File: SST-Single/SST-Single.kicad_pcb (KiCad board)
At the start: 2 copper layers, 62 x 24 mm, 13 parts, among them J1 MJ-179PH, J2 Conn_01x03_Pin, J3 Conn_01x04_Pin, Q1 2SJ498-D, U1 FT231XS_Breakout, U2 LT1785AxN8

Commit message: Add URL test and team logo to the footprint
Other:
- board text added: "SST-Single github.com/rmf-hru-wg/SerialServoTester"

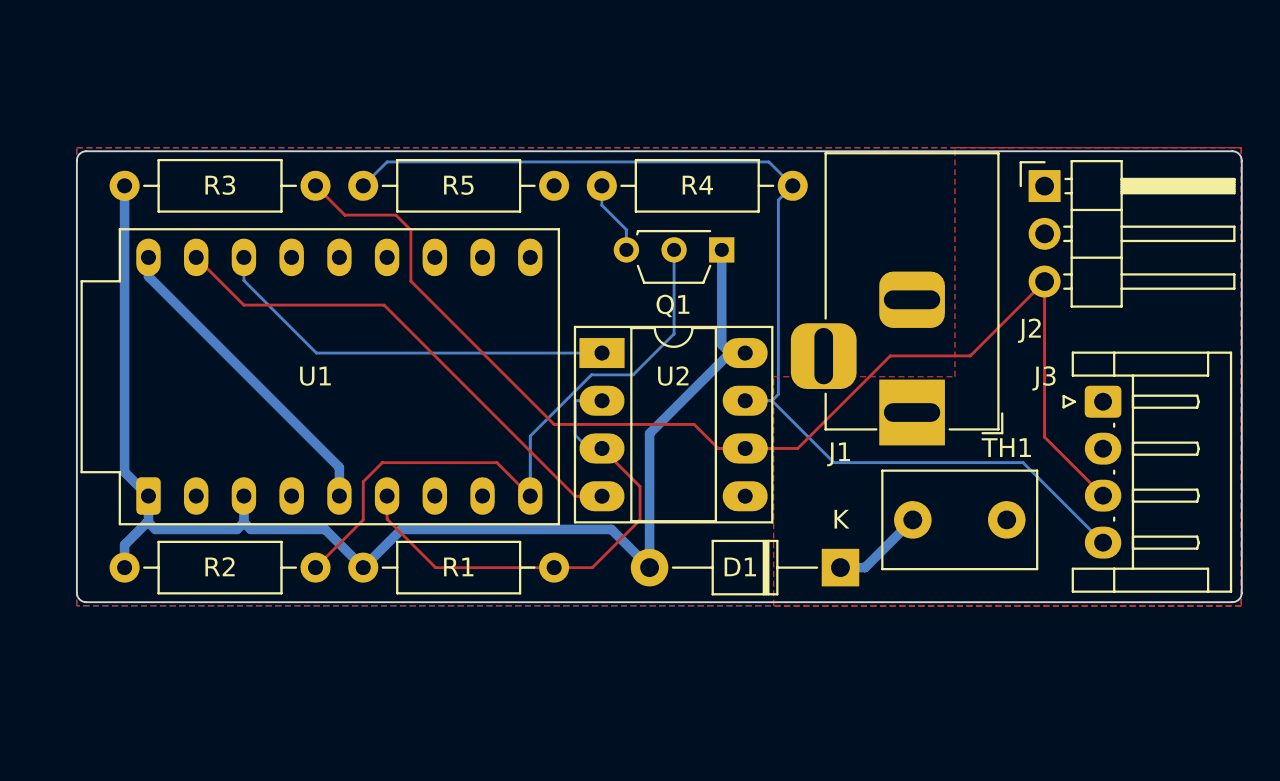
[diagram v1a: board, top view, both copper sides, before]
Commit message: Add DIP switch to select serial mode
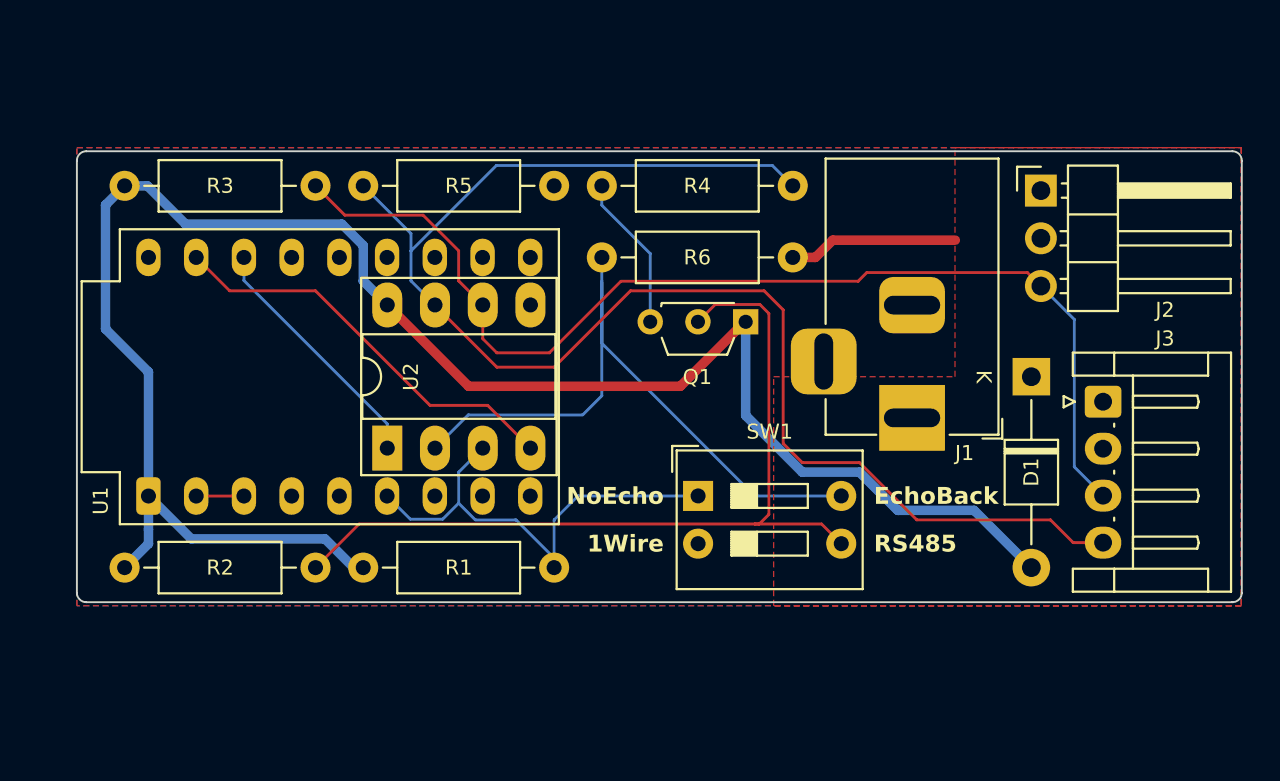
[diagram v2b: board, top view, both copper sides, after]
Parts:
- removed TH1: PTGL07AR820M9A51B0, Capacitor_THT:C_Disc_D8.0mm_W5.0mm_P5.00mm
- added R6: 5.1k, Resistor_THT:R_Axial_DIN0207_L6.3mm_D2.5mm_P10.16mm_Horizontal, F.Cu at (127.9, 55.6)
- added SW1: SW_DIP_x02, Button_Switch_THT:SW_DIP_SPSTx02_Slide_9.78x7.26mm_W7.62mm_P2.54mm, F.Cu at (133.1, 68.3)
- U1: value FT231XS_Breakout -> FT231XS-Breakout
- moved D1 14.4 mm to (150.8, 62.0), turned to -90 degrees
- moved U2 12.5 mm to (116.5, 65.8), turned to 90 degrees
- moved Q1 4.03 mm to (135.6, 59.1)
- moved J2 0.31 mm to (151.3, 52.1)
- moved J1 0.28 mm to (144.4, 64.2)
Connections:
- R1 pad 1: Net-(U1-CBUS0) -> /RXDEN
- U1 pad 2: unconnected-(U1-3V3OUT-Pad2) -> Net-(U1-3V3OUT)
- U1 pad 3: Net-(D1-A) -> Net-(U1-3V3OUT)
- U1 pad 6: Net-(U1-CBUS0) -> /RXDEN
- U1 pad 9: /~{EN_4PIN} -> unconnected-(U1-CBUS3-Pad9)
- U2 pad 2: Net-(U1-CBUS0) -> /~{RS485_RE}
- U2 pad 3: Net-(U1-CBUS0) -> /RXDEN
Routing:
- net /~{RS485_RE}: track 0.00 -> 36.8 mm
- net Net-(D1-A): track 72.2 -> 98.8 mm
- net Net-(U1-CBUS0): track 26.4 -> 0.00 mm
- net /RXDEN: track 0.00 -> 25.7 mm
- net /RS485B: track 58.0 -> 78.9 mm
- net GND: track 16.9 -> 0.00 mm
- net /~{EN_4PIN}: track 33.2 -> 45.4 mm
- net VCC: track 0.00 -> 9.03 mm
- net Net-(U1-RXD): track 21.9 -> 13.3 mm
- net Net-(D1-K): track 4.90 -> 0.00 mm
- net Net-(U1-TXD): track 26.9 -> 22.0 mm
- net Net-(Q1-S): track 3.95 -> 8.30 mm
- net /RS485A: track 62.6 -> 58.9 mm
- net Net-(U1-3V3OUT): track 0.00 -> 2.54 mm
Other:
- board text added: "1Wire"
- board text added: "EchoBack"
- board text added: "GND VCC A B"
- board text added: "GND VCC SIG"
- board text added: "NoEcho"
- board text added: "RS485"

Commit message: Remove FET and modify resistors of RS485 DE line
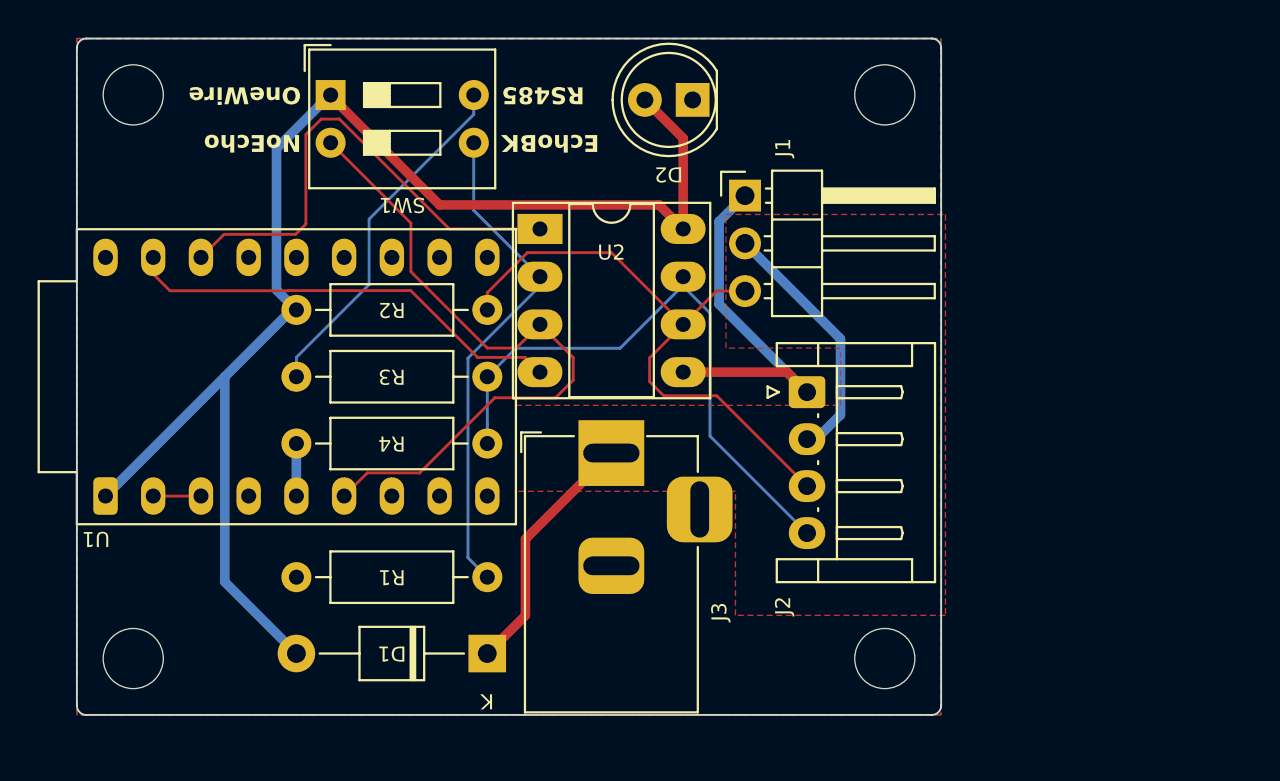
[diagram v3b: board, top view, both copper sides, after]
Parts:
- removed Q1: 2SJ498-D, Package_TO_SOT_THT:TO-92S_Wide
- removed R5, R6: 5.1k, Resistor_THT:R_Axial_DIN0207_L6.3mm_D2.5mm_P10.16mm_Horizontal
- added D2: OSR6LU5B64A-12V, LED_THT:LED_D5.0mm, F.Cu at (132.8, 47.3)
- added H1: MountingHole, MountingHole:MountingHole_3.2mm_M3, F.Cu at (103.0, 47.0)
- added H2: MountingHole, MountingHole:MountingHole_3.2mm_M3, F.Cu at (143.0, 47.0)
- added H3: MountingHole, MountingHole:MountingHole_3.2mm_M3, F.Cu at (143.0, 77.0)
- added H4: MountingHole, MountingHole:MountingHole_3.2mm_M3, F.Cu at (103.0, 77.0)
- J1: value MJ-179PH -> Conn_01x03_Pin; footprint Connector_BarrelJack:BarrelJack_Horizontal -> Connector_PinHeader_2.54mm:PinHeader_1x03_P2.54mm_Horizontal
- J2: value Conn_01x03_Pin -> Conn_01x04_Pin; footprint Connector_PinHeader_2.54mm:PinHeader_1x03_P2.54mm_Horizontal -> Connector_JST:JST_EH_S4B-EH_1x04_P2.50mm_Horizontal
- J3: value Conn_01x04_Pin -> MJ-179PH; footprint Connector_JST:JST_EH_S4B-EH_1x04_P2.50mm_Horizontal -> Connector_BarrelJack:BarrelJack_Horizontal
- SW1: value SW_DIP_x02 -> EDS102SZ
- moved D1 32.5 mm to (121.8, 76.7), turned to 180 degrees
- moved R4 29.8 mm to (111.7, 65.6), turned to 0 degrees
- moved SW1 28.9 mm to (113.5, 47.0)
- moved J3 26.3 mm to (128.4, 66.1), turned to 90 degrees
- moved R2 16.5 mm to (121.8, 58.4)
- moved J2 16.4 mm to (138.9, 62.8), turned to -90 degrees
- moved J1 14.8 mm to (135.6, 52.4), turned to 0 degrees
- moved U2 14.2 mm to (124.6, 54.1), turned to 0 degrees
- moved R1 13.7 mm to (111.7, 72.7), turned to 0 degrees
- moved R3 13.7 mm to (121.8, 62.0)
- moved U1 2.29 mm to (111.7, 62.0)
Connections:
- net Net-(U1-RXD) renamed /RXD
- net Net-(U1-TXD) renamed /TXD
- D1 pad 1: Net-(D1-K) -> VCC
- D1 pad 2: Net-(D1-A) -> +5V
- J1 pad 1: VCC -> GND
- J1 pad 2: GND -> VCC
- J1 pad 3: GND -> /RS485A
- J3 pad 1: GND -> VCC
- J3 pad 2: VCC -> GND
- J3 pad 3: /RS485A -> GND
- R1 pad 1: /RXDEN -> GND
- R1 pad 2: Net-(D1-A) -> /~{RS485_RE}
- R2 pad 1: /~{EN_4PIN} -> /RS485A
- R2 pad 2: Net-(D1-A) -> +5V
- R3 pad 1: /RS485A -> /RS485B
- R3 pad 2: Net-(D1-A) -> /RS485B_UP
- R4 pad 1: /RS485B -> GND
- R4 pad 2: Net-(Q1-S) -> /RS485B
- SW1 pad 1: /RXDEN -> +5V
- SW1 pad 2: GND -> /RXDEN
- SW1 pad 3: /~{EN_4PIN} -> /~{RS485_RE}
- SW1 pad 4: /~{RS485_RE} -> /RS485B_UP
- U1 pad 1: Net-(D1-A) -> +5V
- U2 pad 8: Net-(D1-A) -> +5V
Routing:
- net Net-(D1-A): track 98.8 -> 0.00 mm
- net +5V: track 0.00 -> 73.1 mm
- net /RS485B: track 78.9 -> 33.5 mm
- net /~{EN_4PIN}: track 45.4 -> 0.00 mm
- net /RS485A: track 58.9 -> 32.3 mm
- net GND: track 0.00 -> 22.8 mm
- net /RS485B_UP: track 0.00 -> 18.9 mm
- net VCC: track 9.03 -> 26.9 mm
- net /RXD: track 13.3 -> 26.3 mm
- net /RXDEN: track 25.7 -> 36.2 mm
- net /~{RS485_RE}: track 36.8 -> 26.6 mm
- net Net-(Q1-S): track 8.30 -> 0.00 mm
- net /TXD: track 22.0 -> 23.6 mm
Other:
- board size 62 x 24 mm -> 46 x 36 mm
- board text added: "EchoBK"
- board text added: "OneWire"
- board text removed: "1Wire"
- board text removed: "EchoBack"

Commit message: Update parts layout
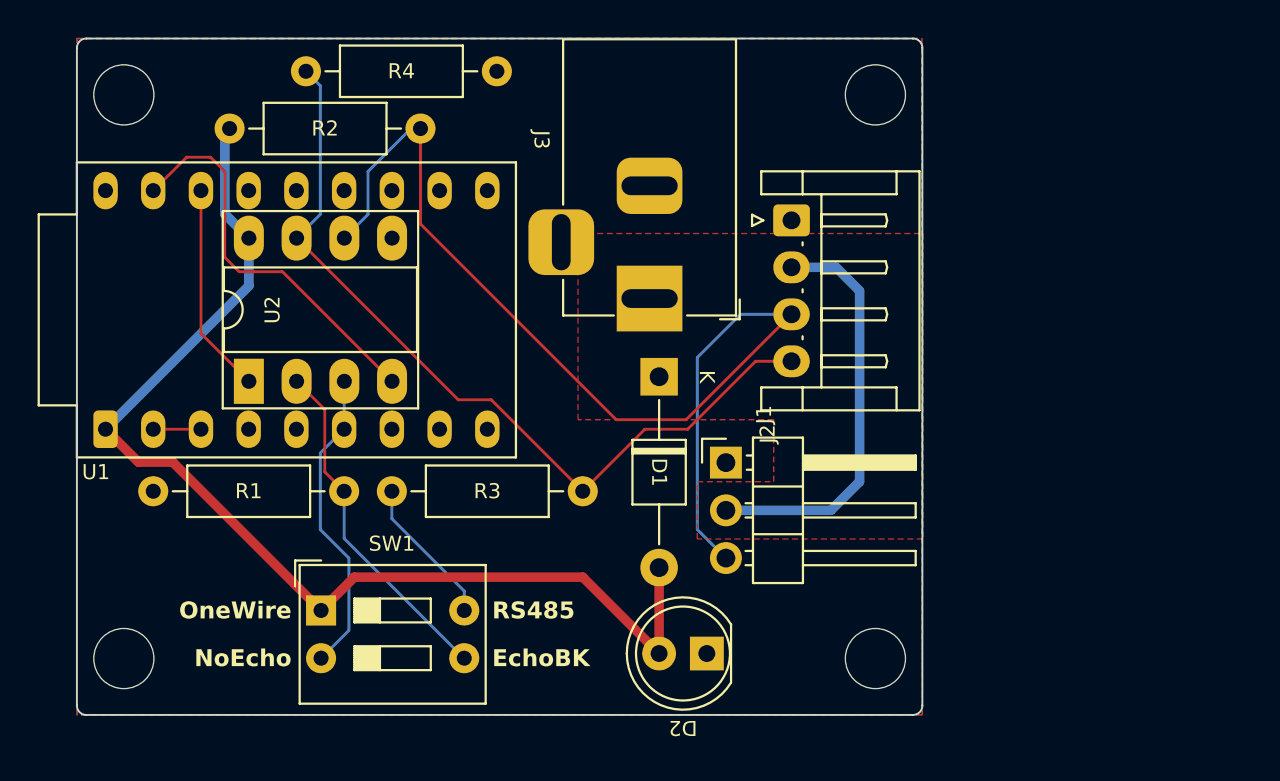
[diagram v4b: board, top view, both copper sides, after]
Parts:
- moved D2 29.5 mm to (133.5, 76.7)
- moved SW1 27.4 mm to (113.0, 74.4)
- moved R4 22.5 mm to (122.4, 45.7), turned to 180 degrees
- moved U2 17.5 mm to (109.2, 62.2), turned to 90 degrees
- moved D1 17.3 mm to (131.0, 62.0), turned to -90 degrees
- moved J1 14.2 mm to (134.5, 66.6)
- moved R2 10.3 mm to (118.3, 48.8)
- moved J2 9.18 mm to (138.0, 53.7)
- moved R1 8.89 mm to (104.1, 68.1)
- moved J3 8.47 mm to (130.5, 57.8), turned to -90 degrees
- moved R3 7.94 mm to (126.9, 68.1)
- moved U1 3.56 mm to (111.7, 58.4)
- moved H1 0.50 mm to (102.5, 47.0)
- moved H2 0.50 mm to (142.5, 47.0)
- moved H3 0.50 mm to (142.5, 77.0)
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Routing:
- net /RS485A: track 32.3 -> 56.5 mm
- net GND: track 22.8 -> 0.00 mm
- net /RXDEN: track 36.2 -> 16.5 mm
- net /RXD: track 26.3 -> 11.2 mm
- net +5V: track 73.1 -> 60.2 mm
- net /RS485B: track 33.5 -> 44.5 mm
- net /RS485B_UP: track 18.9 -> 7.94 mm
- net /~{RS485_RE}: track 26.6 -> 18.4 mm
- net VCC: track 26.9 -> 22.0 mm
- net /TXD: track 23.6 -> 21.1 mm
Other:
- board size 46 x 36 mm -> 45 x 36 mm

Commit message: Update PCB pattern
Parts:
- moved U2 5.08 mm to (114.2, 62.5)
- moved R4 1.14 mm to (123.4, 46.3)
- moved J3 0.79 mm to (131.0, 58.4)
- moved D2 0.51 mm to (133.5, 76.2)
- moved R2 0.51 mm to (118.3, 49.3)
- moved SW1 0.51 mm to (113.0, 73.9)
- moved J1 0.49 mm to (134.5, 66.1)
- moved D1 0.25 mm to (131.0, 61.7)
- moved U1 0.25 mm to (111.7, 58.7)
- moved J2 0.18 mm to (137.9, 53.7)
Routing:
- net /RS485A: track 56.5 -> 41.9 mm
- net VCC: track 22.0 -> 32.6 mm
- net +5V: track 60.2 -> 65.5 mm
- net /RXDEN: track 16.5 -> 21.3 mm
- net /TXD: track 21.1 -> 24.5 mm
- net /RS485B: track 44.5 -> 41.3 mm
- net /RXD: track 11.2 -> 13.3 mm
- net /~{RS485_RE}: track 18.4 -> 17.7 mm
- net /RS485B_UP: track 7.94 -> 7.43 mm
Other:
- board size 45 x 36 mm -> 45 x 35 mm

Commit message: Modify to order slightly
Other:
- board text added: "EchoTX"
- board text removed: "EchoBK"
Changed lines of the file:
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@@
 		)
 	)
-	(gr_text "EchoBK"
+	(gr_text "EchoTX"
 		(at 122.098 76.478 0)
 		(layer "F.SilkS")

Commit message: Add CC-BY logo
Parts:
- added REF**: CC-BY, Symbol:Symbol_CC-Attribution_CopperTop_Small, B.Cu at (127.9, 47.8)
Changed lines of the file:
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@@
+		)
+	)
+	(footprint "Symbol:Symbol_CC-Attribution_CopperTop_Small"
+		(layer "B.Cu")
+		(at 127.94 47.776 90)
+		(descr "Creative Commons symbol, CC-BY, copper layer, 5mm")
+		(property "Reference" "REF**"
+			(at 0 4 270)
+			(layer "B.SilkS")
+			(hide yes)
+			(effects
+				(font
+					(size 1 1)
+					(thickness 0.15)
+				)
+				(justify mirror)
+			)
+		)
+		(property "Value" "CC-BY"
+			(at 0 4.064 270)
+			(unlocked yes)
+			(layer "B.SilkS")
+			(effects
+				(font
+					(size 1 1)
+					(thickness 0.15)
+				)
+				(justify mirror)
+			)
+		)
+		(property "Footprint" "Symbol:Symbol_CC-Attribution_CopperTop_Small"
+			(at 0 0 -90)
+			(unlocked yes)
+			(layer "B.Fab")
+			(hide yes)
+			(effects
+				(font
+					(size 1.27 1.27)
+				)
+				(justify mirror)
+			)
+		)
+		(property "Datasheet" ""
+			(at 0 0 -90)
+			(unlocked yes)
+			(layer "B.Fab")
+			(hide yes)
+			(effects
+				(font
+					(size 1.27 1.27)
+				)
+				(justify mirror)
+			)
+		)
+		(property "Description" ""
+			(at 0 0 -90)
+			(unlocked yes)
+			(layer "B.Fab")
+			(hide yes)
+			(effects
+				(font
+					(size 1.27 1.27)
+				)
+				(justify mirror)
+			)
+		)
+		(attr exclude_from_pos_files exclude_from_bom allow_missing_courtyard)
+		(fp_rect
+			(start 0.45 -1.85)
+			(end -0.45 0)
+			(stroke
+				(width 0)
+				(type solid)
+			)
+			(fill solid)
+			(layer "B.SilkS")
+		)
+		(fp_rect
+			(start 0.8 -0.4)
+			(end -0.8 -0.2)
+			(stroke
+				(width 0)
+				(type solid)
+			)
+			(fill solid)
+			(layer "B.SilkS")
+		)
+		(fp_rect
+			(start 0.6 -0.2)
+			(end -0.6 0.8)
+			(stroke
+				(width 0.4)
+				(type solid)
+			)
+			(fill solid)
+			(layer "B.SilkS")
+		)
+		(fp_circle
+			(center 0.00064 0)
+			(end 2.50064 0)
+			(stroke
+				(width 0.4)
+				(type default)
+			)
+			(fill none)
+			(layer "B.SilkS")
+		)
+		(fp_circle
+			(center 0 1.59)
+			(end 0.3 1.59)
+			(stroke
+				(width 0.2)
+				(type solid)
+			)
+			(fill solid)
+			(layer "B.SilkS")
 		)
 	)
